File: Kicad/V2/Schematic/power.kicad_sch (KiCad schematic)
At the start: 15 parts, among them J3 Conn_USB_Receptacle, U3 AMS1117

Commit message: ajout perle ferrite et fusible polymer
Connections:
- net VBUS: no longer C11.1, C14.1, D3.1 (A), U3.3 (Vin)
- new net VCC: C11.1, C14.1, U3.3 (Vin)
- new net VCCL: D3.1 (A)
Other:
- moved on the sheet: C11, C12, J3, R13, R15, R16

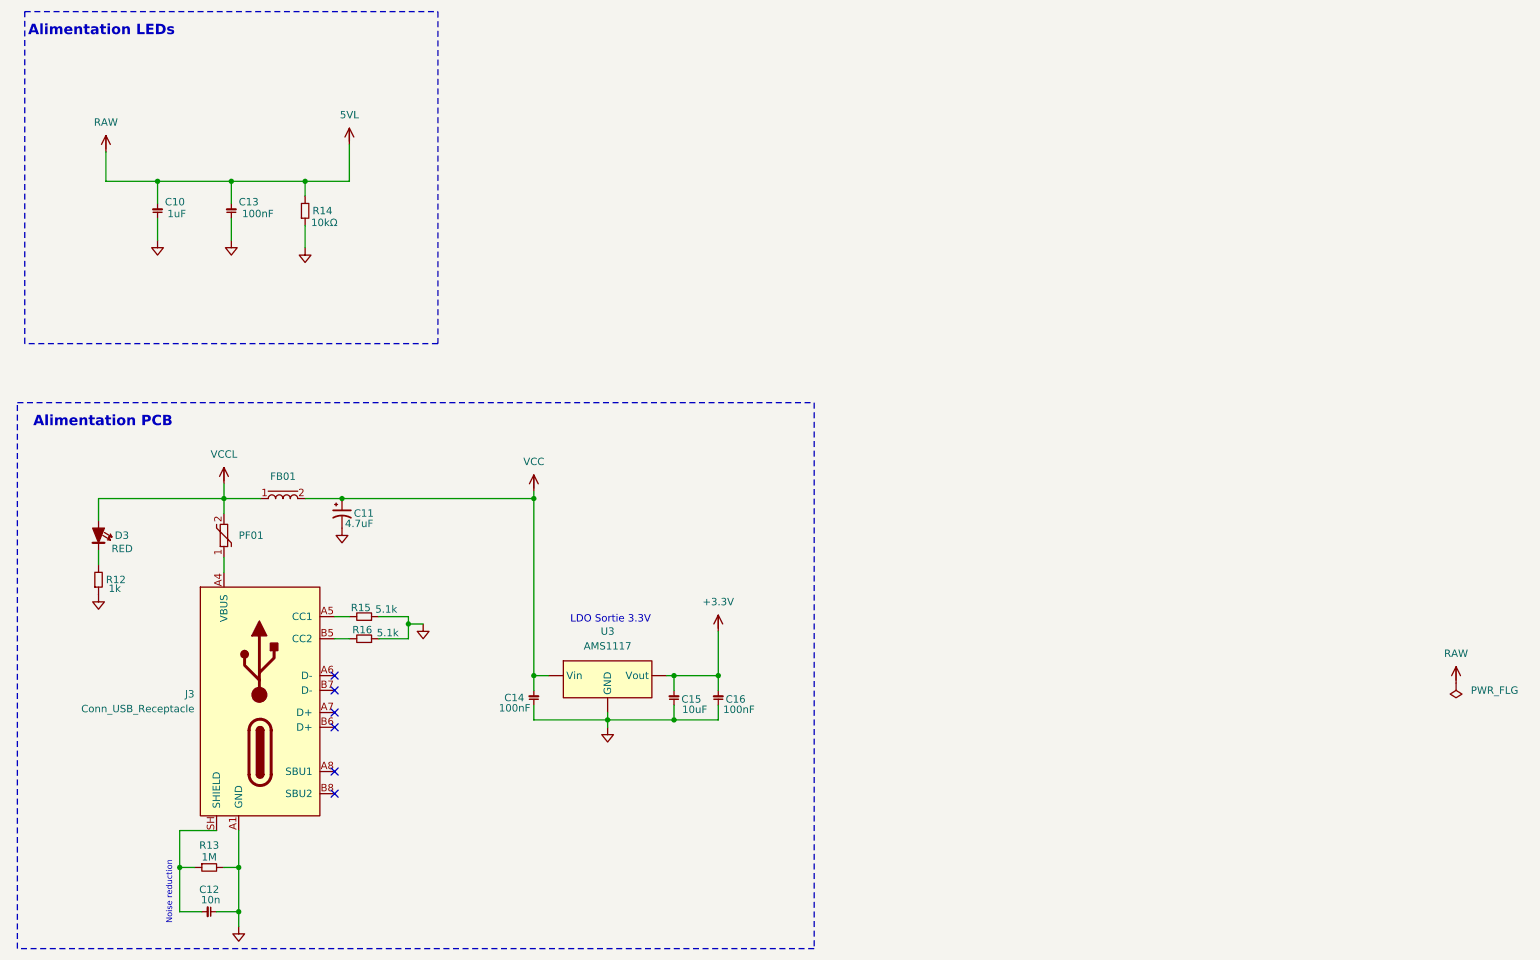
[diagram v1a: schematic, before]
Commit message: Alimentation finalisée & blindage connecteur FPC
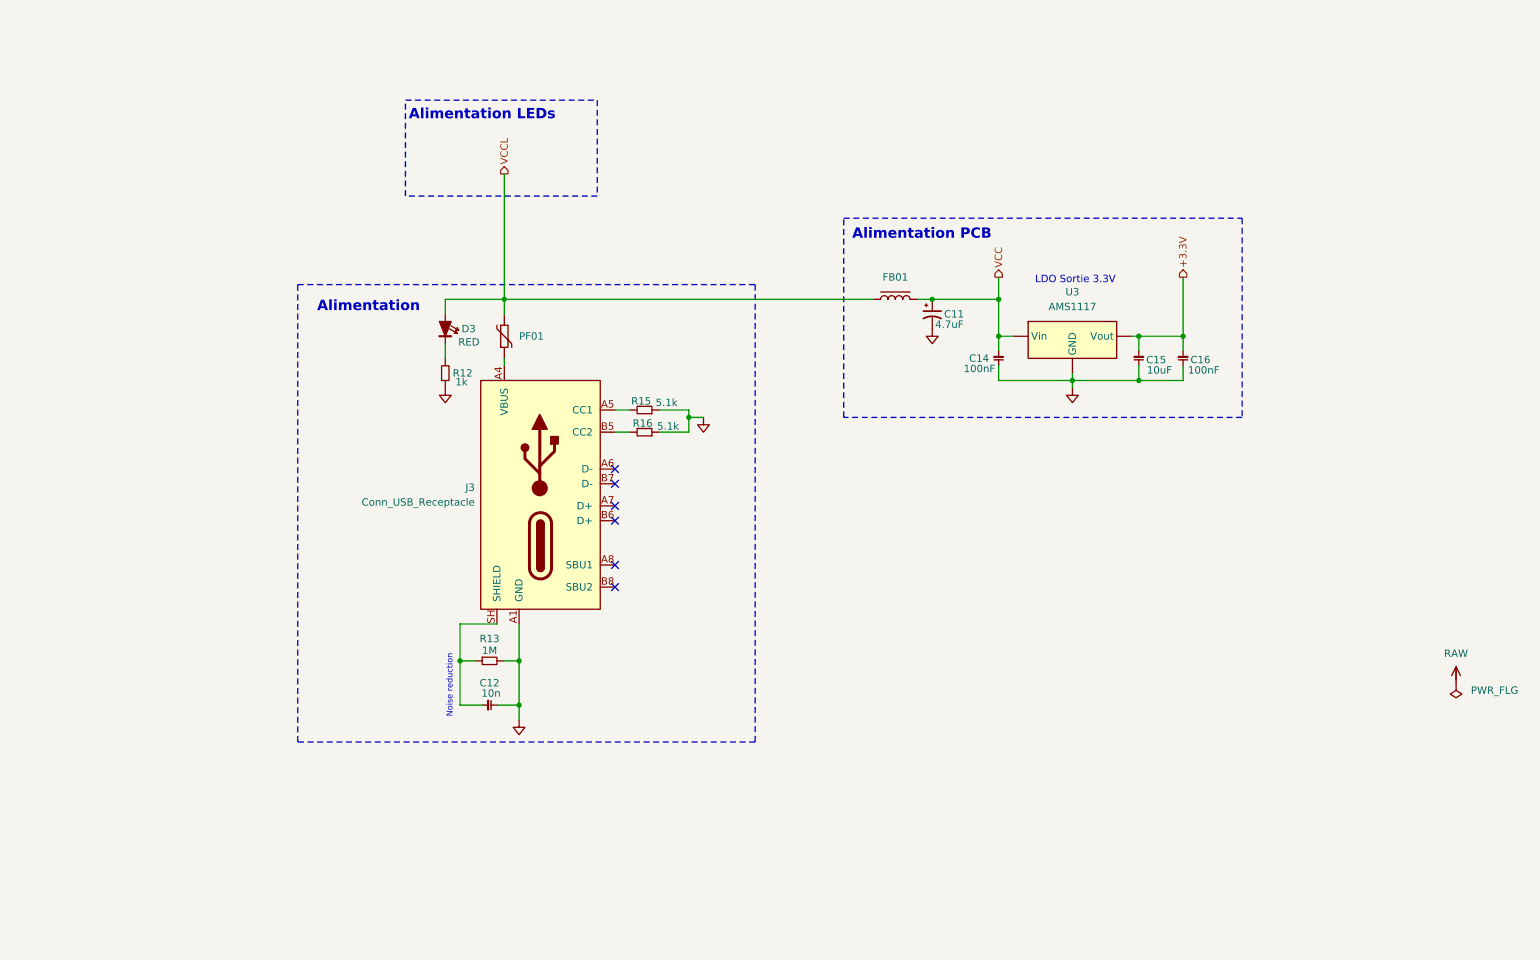
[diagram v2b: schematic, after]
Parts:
- removed C10: 1uF, MyGlove:Capacitor_0603, symbol G-Love:C
- removed C13: 100nF, MyGlove:Capacitor_0603, symbol G-Love:C
- removed R14: 10kΩ, MyGlove:Resistor_0603, symbol G-Love:R
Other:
- note added: "Alimentation"
- moved on the sheet: C11, C12, C14, C15, C16, D3, J3, R12, R13, R15, R16, U3

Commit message: New footprints : Ferrite bead, poly fuse, TVS diode. To do: FPC connector footprint
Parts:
- renumbered C12 to C10, C14 to C12, C15 to C13, C16 to C14, D3 to D7, J3 to J_1, R12 to R14, R13 to R15, R15 to R16, R16 to R17
